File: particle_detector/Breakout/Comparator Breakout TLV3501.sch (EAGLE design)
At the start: 4 parts

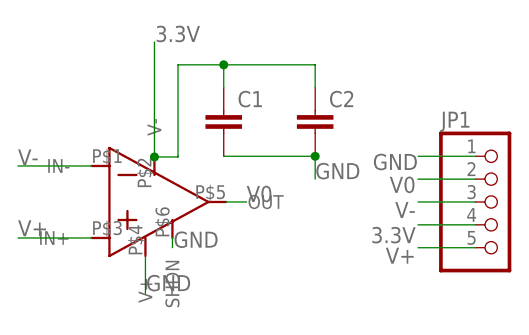
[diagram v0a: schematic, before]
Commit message: Fixed problematic TLVInsect comparator
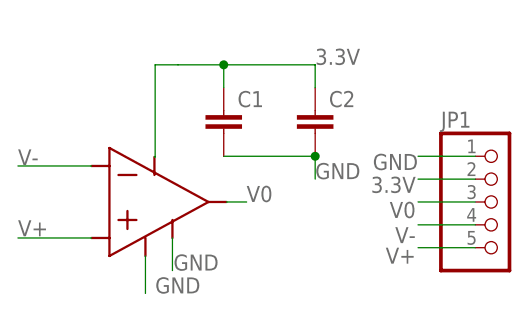
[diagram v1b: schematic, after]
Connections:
- net 3.3V: now also JP1.2, U$1.V+; no longer JP1.4, U$1.V-
- net GND: now also U$1.V-; no longer U$1.V+
- net V-: now also JP1.4; no longer JP1.3
- net V0: now also JP1.3; no longer JP1.2
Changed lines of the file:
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@@
 </segment>
 <segment>
-<pinref part="JP1" gate="A" pin="3"/>
-<wire x1="38.1" y1="0" x2="31.75" y2="0" width="0.1524" layer="91"/>
-<label x="31.496" y="0" size="1.778" layer="95" rot="R180"/>
+<pinref part="JP1" gate="A" pin="4"/>
+<wire x1="38.1" y1="-2.54" x2="31.75" y2="-2.54" width="0.1524" layer="91"/>
+<label x="31.496" y="-2.794" size="1.778" layer="95" rot="R180"/>
 </segment>
 </net>
@@
 </segment>
 <segment>
-<pinref part="JP1" gate="A" pin="2"/>
-<wire x1="38.1" y1="2.54" x2="31.75" y2="2.54" width="0.1524" layer="91"/>
-<label x="31.496" y="2.794" size="1.778" layer="95" rot="R180"/>
+<pinref part="JP1" gate="A" pin="3"/>
+<wire x1="38.1" y1="0" x2="31.75" y2="0" width="0.1524" layer="91"/>
+<label x="31.496" y="0" size="1.778" layer="95" rot="R180"/>
 </segment>
 </net>
@@
 <net name="3.3V" class="0">
 <segment>
-<pinref part="JP1" gate="A" pin="4"/>
-<wire x1="38.1" y1="-2.54" x2="31.75" y2="-2.54" width="0.1524" layer="91"/>
-<label x="31.496" y="-2.794" size="1.778" layer="95" rot="R180"/>
-</segment>
-<segment>
-<pinref part="U$1" gate="G$1" pin="V-"/>
-<wire x1="2.46" y1="5" x2="2.46" y2="17.78" width="0.1524" layer="91"/>
-<label x="2.54" y="17.78" size="1.778" layer="95"/>
 <wire x1="10.16" y1="15.24" x2="20.32" y2="15.24" width="0.1524" layer="91"/>
 <wire x1="10.16" y1="15.24" x2="10.16" y2="12.7" width="0.1524" layer="91"/>
@@
 <wire x1="10.16" y1="15.24" x2="5.08" y2="15.24" width="0.1524" layer="91"/>
 <junction x="10.16" y="15.24"/>
-<wire x1="5.08" y1="15.24" x2="5.08" y2="5.08" width="0.1524" layer="91"/>
-<wire x1="5.08" y1="5.08" x2="5.08" y2="5" width="0.1524" layer="91"/>
-<wire x1="5.08" y1="5" x2="2.46" y2="5" width="0.1524" layer="91"/>
-<junction x="2.46" y="5"/>
+<pinref part="U$1" gate="G$1" pin="V+"/>
+<wire x1="2.46" y1="5" x2="2.54" y2="5" width="0.1524" layer="91"/>
+<wire x1="2.54" y1="5" x2="2.54" y2="15.24" width="0.1524" layer="91"/>
+<wire x1="2.54" y1="15.24" x2="5.08" y2="15.24" width="0.1524" layer="91"/>
+<label x="20.32" y="15.24" size="1.778" layer="95"/>
+</segment>
+<segment>
+<pinref part="JP1" gate="A" pin="2"/>
+<wire x1="38.1" y1="2.54" x2="31.75" y2="2.54" width="0.1524" layer="91"/>
+<label x="31.496" y="2.794" size="1.778" layer="95" rot="R180"/>
 </segment>
 </net>
 <net name="GND" class="0">
 <segment>
-<pinref part="U$1" gate="G$1" pin="V+"/>
-<wire x1="1.46" y1="-6" x2="1.46" y2="-10.16" width="0.1524" layer="91"/>
-<label x="1.524" y="-9.906" size="1.778" layer="95"/>
-</segment>
-<segment>
 <pinref part="U$1" gate="G$1" pin="SHDN"/>
-<wire x1="4.46" y1="-4" x2="4.46" y2="-5.08" width="0.1524" layer="91"/>
-<label x="4.572" y="-5.08" size="1.778" layer="95"/>
+<wire x1="4.46" y1="-4" x2="4.46" y2="-7.62" width="0.1524" layer="91"/>
+<label x="4.572" y="-7.62" size="1.778" layer="95"/>
 </segment>
 <segment>
@@
 <label x="31.75" y="5.334" size="1.778" layer="95" rot="R180"/>
 </segment>
+<segment>
+<pinref part="U$1" gate="G$1" pin="V-"/>
+<wire x1="1.46" y1="-6" x2="1.46" y2="-10.16" width="0.1524" layer="91"/>
+<label x="2.54" y="-10.16" size="1.778" layer="95"/>
+</segment>
 </net>
